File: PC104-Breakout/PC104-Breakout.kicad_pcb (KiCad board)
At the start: 2 copper layers, 175 x 131 mm, 59 parts, among them J1 H1-02x26_Even, J10 Conn_01x02, J11 Conn_01x03_Socket, J12 Conn_01x03_Socket, J13 Conn_01x03_Socket, J2 H1-02x26_Odd, J3 H2-0x26_Even, J4 H2-0x26_Odd, J5 Screw_Terminal_01x02, J6 Screw_Terminal_01x02, J7 Screw_Terminal_01x02, J8 Conn_01x02, J9 Conn_01x02, M1 MountingHole_Pad, M10 MountingHole_Pad, M11 MountingHole_Pad, M12 MountingHole_Pad, M2 MountingHole_Pad, M3 MountingHole_Pad, M4 MountingHole_Pad, M5 MountingHole_Pad, M6 MountingHole_Pad, M7 MountingHole_Pad, M8 MountingHole_Pad, M9 MountingHole_Pad

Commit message: Polish silkscreen more
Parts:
- moved R1 0.50 mm to (85.5, 33.0)
- moved R2 0.50 mm to (239.5, 33.0)
- moved R3 0.50 mm to (239.5, 154.0)
- moved R4 0.50 mm to (80.0, 148.5)
- moved R5 0.50 mm to (110.0, 125.5)
- moved R6 0.50 mm to (213.0, 114.5)
- moved R7 0.50 mm to (213.0, 35.5)
- moved R8 0.50 mm to (110.0, 37.5)
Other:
- board text added: "< Socket > < Header >"
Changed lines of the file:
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@@
 		(tags "Through hole socket strip THT 1x03 2.54mm single row")
 		(property "Reference" "J13"
-			(at 0 -2.77 360)
+			(at 0 -2.77 0)
 			(layer "F.SilkS")
 			(effects
@@
 		)
 		(property "Value" "Conn_01x03_Socket"
-			(at 0 7.85 360)
+			(at 0 7.85 0)
 			(layer "F.Fab")
 			(effects
@@
 		(tags "LED handsolder")
 		(property "Reference" "D8"
-			(at -2.625 0 360)
+			(at -2.625 0 0)
 			(layer "F.SilkS")
 			(hide yes)
@@
 		)
 		(property "Value" "LED"
-			(at 0 1.43 360)
+			(at 0 1.43 0)
 			(layer "F.Fab")
 			(effects
@@
 		)
 		(fp_text user "${REFERENCE}"
-			(at 0 0 360)
+			(at 0 0 0)
 			(layer "F.Fab")
 			(effects
@@
 			(at 0 -4.2 0)
 			(layer "F.SilkS")
+			(hide yes)
 			(effects
 				(font
@@
 		(tags "LED handsolder")
 		(property "Reference" "D7"
-			(at -2.875 0 360)
+			(at -2.875 0 0)
 			(layer "F.SilkS")
 			(hide yes)
@@
 		)
 		(property "Value" "LED"
-			(at 0 1.43 360)
+			(at 0 1.43 0)
 			(layer "F.Fab")
 			(effects
@@
 		)
 		(fp_text user "${REFERENCE}"
-			(at 0 0 360)
+			(at 0 0 0)
 			(layer "F.Fab")
 			(effects
@@
 			(at 0 -4.2 0)
 			(layer "F.SilkS")
+			(hide yes)
 			(effects
 				(font
@@
 			(at 0 -4.2 0)
 			(layer "F.SilkS")
+			(hide yes)
 			(effects
 				(font
@@
 		(tags "LED handsolder")
 		(property "Reference" "D-H2-26"
-			(at 0 -1.43 360)
+			(at 0 -1.43 0)
 			(layer "F.SilkS")
 			(effects
@@
 		)
 		(property "Value" "LED"
-			(at 0 1.43 360)
+			(at 0 1.43 0)
 			(layer "F.Fab")
 			(effects
@@
 		)
 		(fp_text user "${REFERENCE}"
-			(at 0 0 360)
+			(at 0 0 0)
 			(layer "F.Fab")
 			(effects
@@
 		(tags "LED handsolder")
 		(property "Reference" "D-H2-25"
-			(at 0 -1.43 360)
+			(at 0 -1.43 0)
 			(layer "F.SilkS")
 			(effects
@@
 		)
 		(property "Value" "LED"
-			(at 0 1.43 360)
+			(at 0 1.43 0)
 			(layer "F.Fab")
 			(effects
@@
 		)
 		(fp_text user "${REFERENCE}"
-			(at 0 0 360)
+			(at 0 0 0)
 			(layer "F.Fab")
 			(effects
@@
 		(property "Value" "3k3"
 			(at 0 -1.43 0)
-			(layer "B.Fab")
+			(layer "B.SilkS")
 			(effects
 				(font
@@
 	(footprint "Resistor_SMD:R_0603_1608Metric_Pad0.98x0.95mm_HandSolder"
 		(layer "B.Cu")
-		(at 80 149 180)
+		(at 80 148.5 180)
 		(descr "Resistor SMD 0603 (1608 Metric), square (rectangular) end terminal, IPC_7351 nominal with elongated pad for handsoldering. (Body size source: IPC-SM-782 page 72, https://www.pcb-3d.com/wordpress/wp-content/uploads/ipc-sm-782a_amendment_1_and_2.pdf), generated with kicad-footprint-generator")
 		(tags "resistor handsolder")
@@
 		(property "Value" "10k"
 			(at 0 -1.43 0)
-			(layer "B.Fab")
+			(layer "B.SilkS")
 			(effects
 				(font
@@
 		(property "Value" "5k1"
 			(at 0 -1.43 0)
-			(layer "B.Fab")
+			(layer "B.SilkS")
 			(effects
 				(font
@@
 		(property "Value" "10k"
 			(at 0 -1.43 0)
-			(layer "B.Fab")
+			(layer "B.SilkS")
 			(effects
 				(font
@@
 		(property "Value" "5k1"
 			(at 0 -1.43 0)
-			(layer "B.Fab")
+			(layer "B.SilkS")
 			(effects
 				(font
@@
 	(footprint "Resistor_SMD:R_0603_1608Metric_Pad0.98x0.95mm_HandSolder"
 		(layer "B.Cu")
-		(at 110 125)
+		(at 110 125.5)
 		(descr "Resistor SMD 0603 (1608 Metric), square (rectangular) end terminal, IPC_7351 nominal with elongated pad for handsoldering. (Body size source: IPC-SM-782 page 72, https://www.pcb-3d.com/wordpress/wp-content/uploads/ipc-sm-782a_amendment_1_and_2.pdf), generated with kicad-footprint-generator")
 		(tags "resistor handsolder")
@@
 		(property "Value" "10k"
 			(at 0 -1.43 0)
-			(layer "B.Fab")
+			(layer "B.SilkS")
 			(effects
 				(font
@@
 	(footprint "Resistor_SMD:R_0603_1608Metric_Pad0.98x0.95mm_HandSolder"
 		(layer "B.Cu")
-		(at 240 154 -90)
+		(at 239.5 154 -90)
 		(descr "Resistor SMD 0603 (1608 Metric), square (rectangular) end terminal, IPC_7351 nominal with elongated pad for handsoldering. (Body size source: IPC-SM-782 page 72, https://www.pcb-3d.com/wordpress/wp-content/uploads/ipc-sm-782a_amendment_1_and_2.pdf), generated with kicad-footprint-generator")
 		(tags "resistor handsolder")
@@
 		(property "Value" "10k"
 			(at 0 -1.43 90)
-			(layer "B.Fab")
+			(layer "B.SilkS")
 			(effects
 				(font
@@
 	(footprint "Resistor_SMD:R_0603_1608Metric_Pad0.98x0.95mm_HandSolder"
 		(layer "B.Cu")
-		(at 110 38 180)
+		(at 110 37.5 180)
 		(descr "Resistor SMD 0603 (1608 Metric), square (rectangular) end terminal, IPC_7351 nominal with elongated pad for handsoldering. (Body size source: IPC-SM-782 page 72, https://www.pcb-3d.com/wordpress/wp-content/uploads/ipc-sm-782a_amendment_1_and_2.pdf), generated with kicad-footprint-generator")
 		(tags "resistor handsolder")
@@
 		(property "Value" "10k"
 			(at 0 -1.43 0)
-			(layer "B.Fab")
+			(layer "B.SilkS")
 			(effects
 				(font
@@
 		(property "Value" "10k"
 			(at 0 -1.43 0)
-			(layer "B.Fab")
+			(layer "B.SilkS")
 			(effects
 				(font
@@
 	(footprint "Resistor_SMD:R_0603_1608Metric_Pad0.98x0.95mm_HandSolder"
 		(layer "B.Cu")
-		(at 85 33 90)
+		(at 85.5 33 90)
 		(descr "Resistor SMD 0603 (1608 Metric), square (rectangular) end terminal, IPC_7351 nominal with elongated pad for handsoldering. (Body size source: IPC-SM-782 page 72, https://www.pcb-3d.com/wordpress/wp-content/uploads/ipc-sm-782a_amendment_1_and_2.pdf), generated with kicad-footprint-generator")
 		(tags "resistor handsolder")
@@
 		(property "Value" "10k"
 			(at 0 -1.43 90)
-			(layer "B.Fab")
+			(layer "B.SilkS")
 			(effects
 				(font
@@
 	(footprint "Resistor_SMD:R_0603_1608Metric_Pad0.98x0.95mm_HandSolder"
 		(layer "B.Cu")
-		(at 213 115 180)
+		(at 213 114.5 180)
 		(descr "Resistor SMD 0603 (1608 Metric), square (rectangular) end terminal, IPC_7351 nominal with elongated pad for handsoldering. (Body size source: IPC-SM-782 page 72, https://www.pcb-3d.com/wordpress/wp-content/uploads/ipc-sm-782a_amendment_1_and_2.pdf), generated with kicad-footprint-generator")
 		(tags "resistor handsolder")
@@
 		(property "Value" "10k"
 			(at 0 -1.43 0)
-			(layer "B.Fab")
+			(layer "B.SilkS")
 			(effects
 				(font
@@
 		(property "Value" "5k1"
 			(at 0 -1.43 0)
-			(layer "B.Fab")
+			(layer "B.SilkS")
 			(effects
 				(font
@@
 	(footprint "Resistor_SMD:R_0603_1608Metric_Pad0.98x0.95mm_HandSolder"
 		(layer "B.Cu")
-		(at 213 36 180)
+		(at 213 35.5 180)
 		(descr "Resistor SMD 0603 (1608 Metric), square (rectangular) end terminal, IPC_7351 nominal with elongated pad for handsoldering. (Body size source: IPC-SM-782 page 72, https://www.pcb-3d.com/wordpress/wp-content/uploads/ipc-sm-782a_amendment_1_and_2.pdf), generated with kicad-footprint-generator")
 		(tags "resistor handsolder")
@@
 		(property "Value" "10k"
 			(at 0 -1.43 0)
-			(layer "B.Fab")
+			(layer "B.SilkS")
 			(effects
 				(font
@@
 	(footprint "Resistor_SMD:R_0603_1608Metric_Pad0.98x0.95mm_HandSolder"
 		(layer "B.Cu")
-		(at 240 33 -90)
+		(at 239.5 33 -90)
 		(descr "Resistor SMD 0603 (1608 Metric), square (rectangular) end terminal, IPC_7351 nominal with elongated pad for handsoldering. (Body size source: IPC-SM-782 page 72, https://www.pcb-3d.com/wordpress/wp-content/uploads/ipc-sm-782a_amendment_1_and_2.pdf), generated with kicad-footprint-generator")
 		(tags "resistor handsolder")
@@
 		(property "Value" "10k"
 			(at 0 -1.43 90)
-			(layer "B.Fab")
+			(layer "B.SilkS")
 			(effects
 				(font
@@
 		(property "Value" "3k3"
 			(at 0 -1.43 0)
-			(layer "B.Fab")
+			(layer "B.SilkS")
 			(effects
 				(font
@@
 		(tags "resistor handsolder")
 		(property "Reference" "R16"
-			(at 0 1.43 360)
+			(at 0 1.43 0)
 			(layer "B.SilkS")
 			(effects
@@
 		)
 		(property "Value" "3k3"
-			(at 0 -1.43 360)
-			(layer "B.Fab")
+			(at 0 -1.43 0)
+			(layer "B.SilkS")
 			(effects
 				(font
@@
 		)
 		(fp_text user "${REFERENCE}"
-			(at 0 0 360)
+			(at 0 0 0)
 			(layer "B.Fab")
 			(effects
@@
 	)
 	(gr_rect
+		(start 79 83.5)
+		(end 93 118.5)
+		(stroke
+			(width 0.1)
+			(type solid)
+		)
+		(fill solid)
+		(layer "B.SilkS")
+	)
+	(gr_rect
 		(start 155 47)
 		(end 190 61)
@@
 	)
 	(gr_rect
+		(start 79 83.5)
+		(end 93 118.5)
+		(stroke
+			(width 0.1)
+			(type solid)
+		)
+		(fill solid)
+		(layer "F.SilkS")
+	)
+	(gr_rect
 		(start 75 28)
 		(end 250 159)
@@
 		(layer "Edge.Cuts")
 	)
+	(gr_text "< Socket >\n< Header >"
+		(at 162 137.5 0)
+		(layer "B.SilkS")
+		(effects
+			(font
+				(size 1.5 1)
+				(thickness 0.2)
+				(bold yes)
+			)
+			(justify mirror)
+		)
+	)
+	(gr_text "GND"
+		(at 224 117 -90)
+		(layer "B.SilkS")
+		(effects
+			(font
+				(size 3 3)
+				(thickness 0.6)
+				(bold yes)
+			)
+			(justify bottom mirror)
+		)
+	)
+	(gr_text "3V3"
+		(at 224 41.5 -90)
+		(layer "B.SilkS")
+		(effects
+			(font
+				(size 3 3)
+				(thickness 0.6)
+				(bold yes)
+			)
+			(justify bottom mirror)
+		)
+	)
+	(gr_text "< Socket >\n< Header >"
+		(at 162 151.5 0)
+		(layer "B.SilkS")
+		(effects
+			(font
+				(size 1.5 1)
+				(thickness 0.2)
+				(bold yes)
+			)
+			(justify mirror)
+		)
+	)
 	(gr_text "PC104 Breakout\nRev 3\n2025-02-02"
 		(at 189.5 86 0)
@@
 		)
 	)
+	(gr_text "5V"
+		(at 224 78.5 -90)
+		(layer "B.SilkS")
+		(effects
+			(font
+				(size 3 3)
+				(thickness 0.6)
+				(bold yes)
+			)
+			(justify bottom mirror)
+		)
+	)

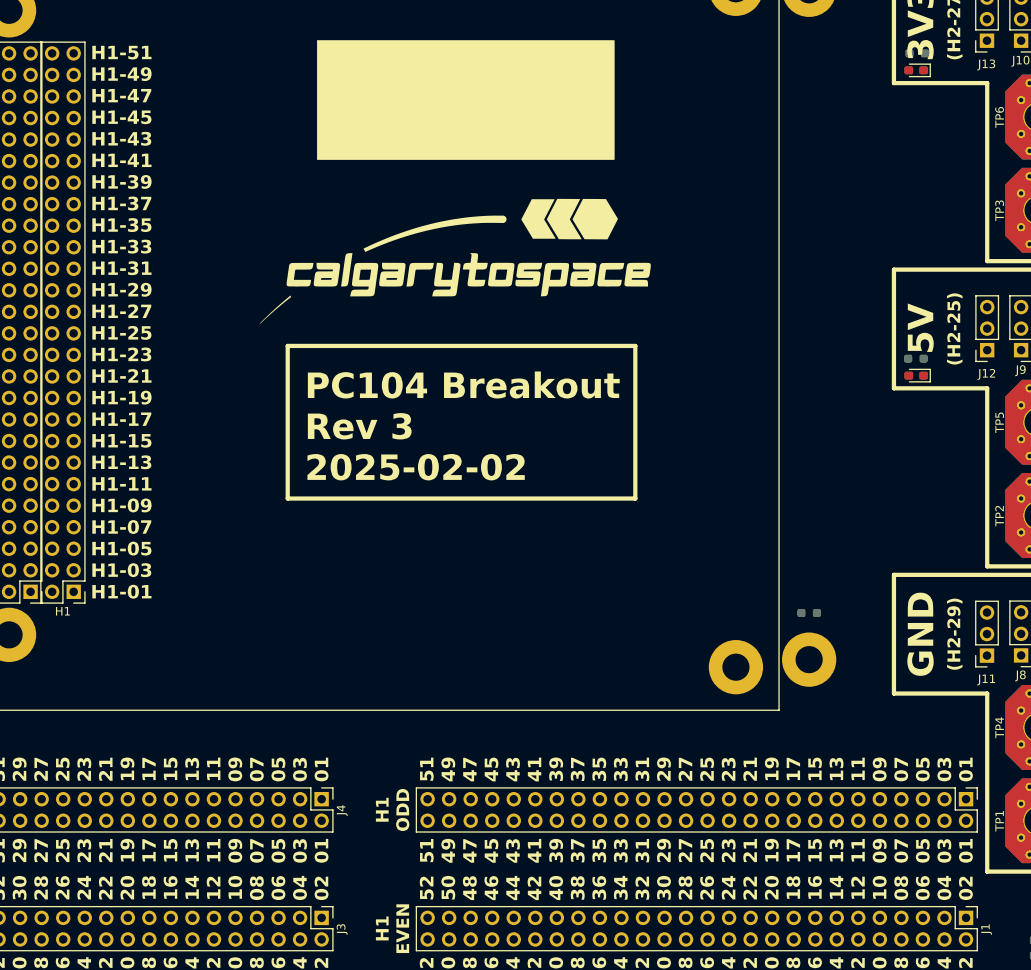
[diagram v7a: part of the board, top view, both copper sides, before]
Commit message: Route H1 breakout
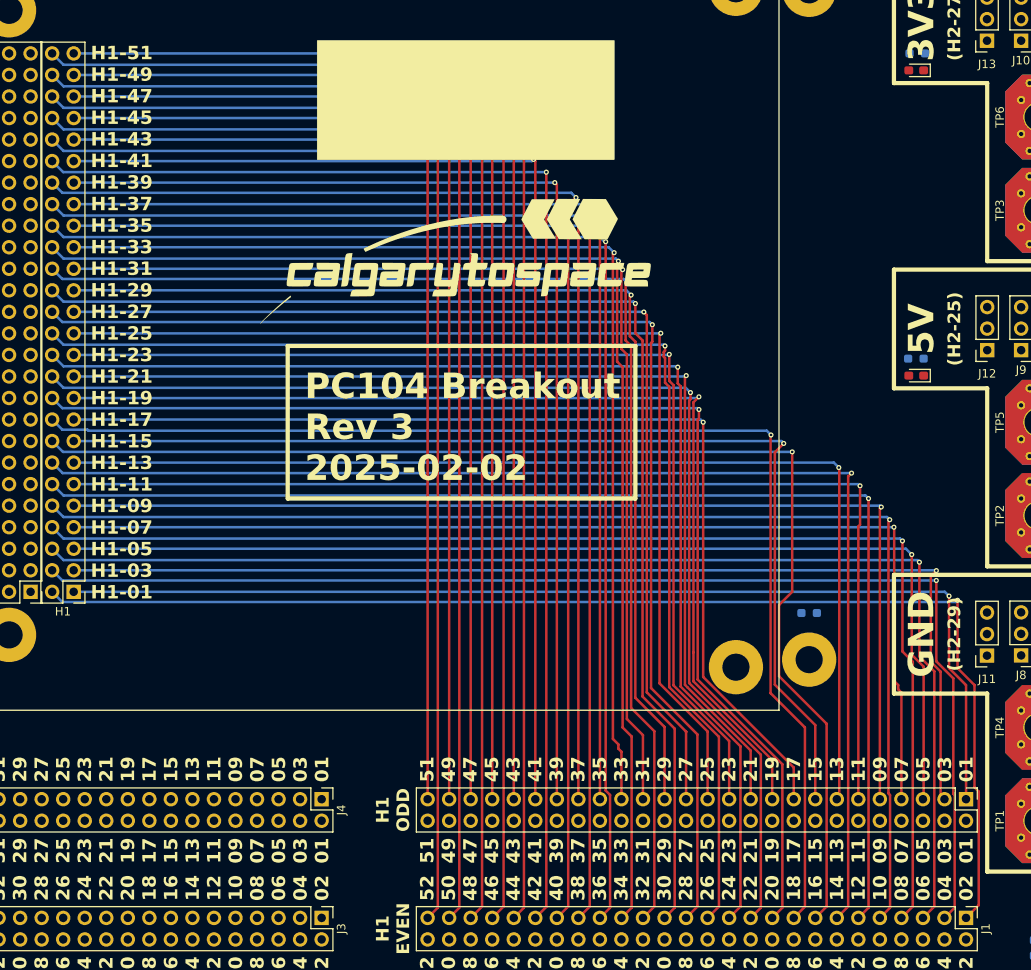
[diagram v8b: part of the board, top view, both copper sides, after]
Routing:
- net H1-40: track 0.00 -> 148.4 mm, vias 0 -> 1
- net H1-14: track 0.00 -> 148.0 mm, vias 0 -> 1
- net H1-48: track 0.00 -> 147.8 mm, vias 0 -> 1
- net H1-38: track 0.00 -> 147.7 mm, vias 0 -> 1
- net H1-42: track 0.00 -> 147.3 mm, vias 0 -> 1
- net H1-46: track 0.00 -> 147.2 mm, vias 0 -> 1
- net H1-10: track 0.00 -> 147.1 mm, vias 0 -> 1
- net H1-44: track 0.00 -> 146.9 mm, vias 0 -> 1
- net H1-12: track 0.00 -> 146.9 mm, vias 0 -> 1
- net H1-52: track 0.00 -> 146.9 mm, vias 0 -> 1
- net H1-50: track 0.00 -> 146.7 mm, vias 0 -> 1
- net H1-36: track 0.00 -> 146.5 mm, vias 0 -> 1
- net H1-02: track 0.00 -> 146.5 mm, vias 0 -> 1
- net H1-08: track 0.00 -> 146.5 mm, vias 0 -> 1
- net H1-16: track 0.00 -> 146.3 mm, vias 0 -> 1
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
